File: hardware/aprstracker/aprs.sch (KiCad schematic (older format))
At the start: 98 parts

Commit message: [HW] Update schematics
Signed-off-by: Angel Hitov <angelhitov@gmail.com>
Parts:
- removed C? (x2): C, ~, symbol C
- removed R? (x2): R, ~, symbol R
- added C? (x15): C, ~, symbol C
- added C? (x2): CTRIM, ~, symbol CTRIM
- added C?: CAPAPOL, ~, symbol CAPAPOL
- added L? (x7): INDUCTOR, ~, symbol INDUCTOR
- added P?: BNC, ~, symbol BNC
- added Q?: NPN, ~, symbol NPN
- added R?: R, ~, symbol R
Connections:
- net labels removed: VRF
- wire segments 174 -> 183
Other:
- moved on the sheet: C?, Q?, R?

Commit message: [HW] Schematic update
Signed-off-by: Angel Hitov <angelhitov@gmail.com>
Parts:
- removed C? (x2): C, ~, symbol C
- removed L?: INDUCTOR, ~, symbol INDUCTOR
- removed P? (x2): BNC, ~, symbol BNC
- removed R? (x2): R, ~, symbol R
- added J1, J?: SMA, SMA, symbol SMA
- added L6: INDUCTOR, ~, symbol INDUCTOR
- added Q2: NPN, ~, symbol NPN
- added R14, R18: R, ~, symbol R
- Q3: renamed from Q?; value PNP -> BCX56
- Q4, Q5: renamed from Q?; value NPN -> BFR93A
- Q6: renamed from Q?; value NPN -> BFG135
- gave numbers to parts that had none: 111
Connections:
- net labels added: RF_EN
- net labels removed: VCO_EN
- wire segments 183 -> 187
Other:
- moved on the sheet: C19, Q3, R17, R20

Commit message: [HW] Kicad project adjustments
Signed-off-by: Angel Hitov <angelhitov@gmail.com>
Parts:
- gave numbers to parts that had none: 1
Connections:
- net CL is gone; now on net CE: U1.4 (CL)
- net CE: now also IC1.12 ((ICP)PB0), IC1.13 ((OC1A)PB1)
- net DATA: now also IC1.14 ((~SS~/OC1B)PB2)
- net GND: now also C48.2
- net at C16.1, C17.1, C18.1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: no longer R24.1
- net at Q5.1 (E), R26.1: now also R24.1
- no-connect marks 0 -> 24
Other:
- moved on the sheet: R24

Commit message: [HW] Schematics/footprints update
Signed-off-by: Angel Hitov <angelhitov@gmail.com>
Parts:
- removed U3: 78L33, ~, symbol 78L05
- removed U4: 78L05, ~, symbol 78L05
- added U3: 78L33, symbol 78LXX
- added U4: 78L05, symbol 78LXX
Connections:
- net +5V: now also U3.3 (VI)
- net GND: now also U3.2 (GND), U4.2 (GND)
- net VCC: now also U4.1 (VO)
- net VDD: now also U4.3 (VI)
- net at C43.1, C45.1, L15.1: now also U3.1 (VO)
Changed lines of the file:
@@
 LIBS:EB-3531
 LIBS:sma
+LIBS:78LXX_SMD
+LIBS:aprs
 LIBS:aprs-cache
 EELAYER 24 0
@@
 RF_EN
 $Comp
-L 78L05 U4
-U 1 1 51A2033B
-P 13550 1950
-F 0 "U4" H 13700 1754 60  0000 C CNN
-F 1 "78L05" H 13550 2150 60  0000 C CNN
-F 2 "~" H 13550 1950 60  0000 C CNN
-F 3 "~" H 13550 1950 60  0000 C CNN
-	1    13550 1950
-	1    0    0    -1
-$EndComp
-$Comp
 L CONN_2 P3
 U 1 1 51A20CAC
@@
 F 3 "~" H 13100 2200 300 0000 C CNN
 	1    13100 2200
-	1    0    0    -1
-$EndComp
-$Comp
-L 78L05 U3
-U 1 1 51A21285
-P 12150 2900
-F 0 "U3" H 12300 2704 60  0000 C CNN
-F 1 "78L33" H 12150 3100 60  0000 C CNN
-F 2 "~" H 12150 2900 60  0000 C CNN
-F 3 "~" H 12150 2900 60  0000 C CNN
-	1    12150 2900
 	1    0    0    -1
 $EndComp
@@
 Wire Wire Line
 	14250 1950 14250 1900
+$Comp
+L 78LXX U4
+U 1 1 51AB80B0
+P 13550 1950
+F 0 "U4" H 13700 1754 60  0000 C CNN
+F 1 "78L05" H 13550 2150 60  0000 C CNN
+F 2 "" H 13550 1950 60  0000 C CNN
+F 3 "" H 13550 1950 60  0000 C CNN
+	1    13550 1950
+	1    0    0    -1
+$EndComp
+$Comp
+L 78LXX U3
+U 1 1 51AB8477
+P 12150 2900
+F 0 "U3" H 12300 2704 60  0000 C CNN
+F 1 "78L33" H 12150 3100 60  0000 C CNN
+F 2 "" H 12150 2900 60  0000 C CNN
+F 3 "" H 12150 2900 60  0000 C CNN
+	1    12150 2900
+	1    0    0    -1
+$EndComp
 $EndSCHEMATC

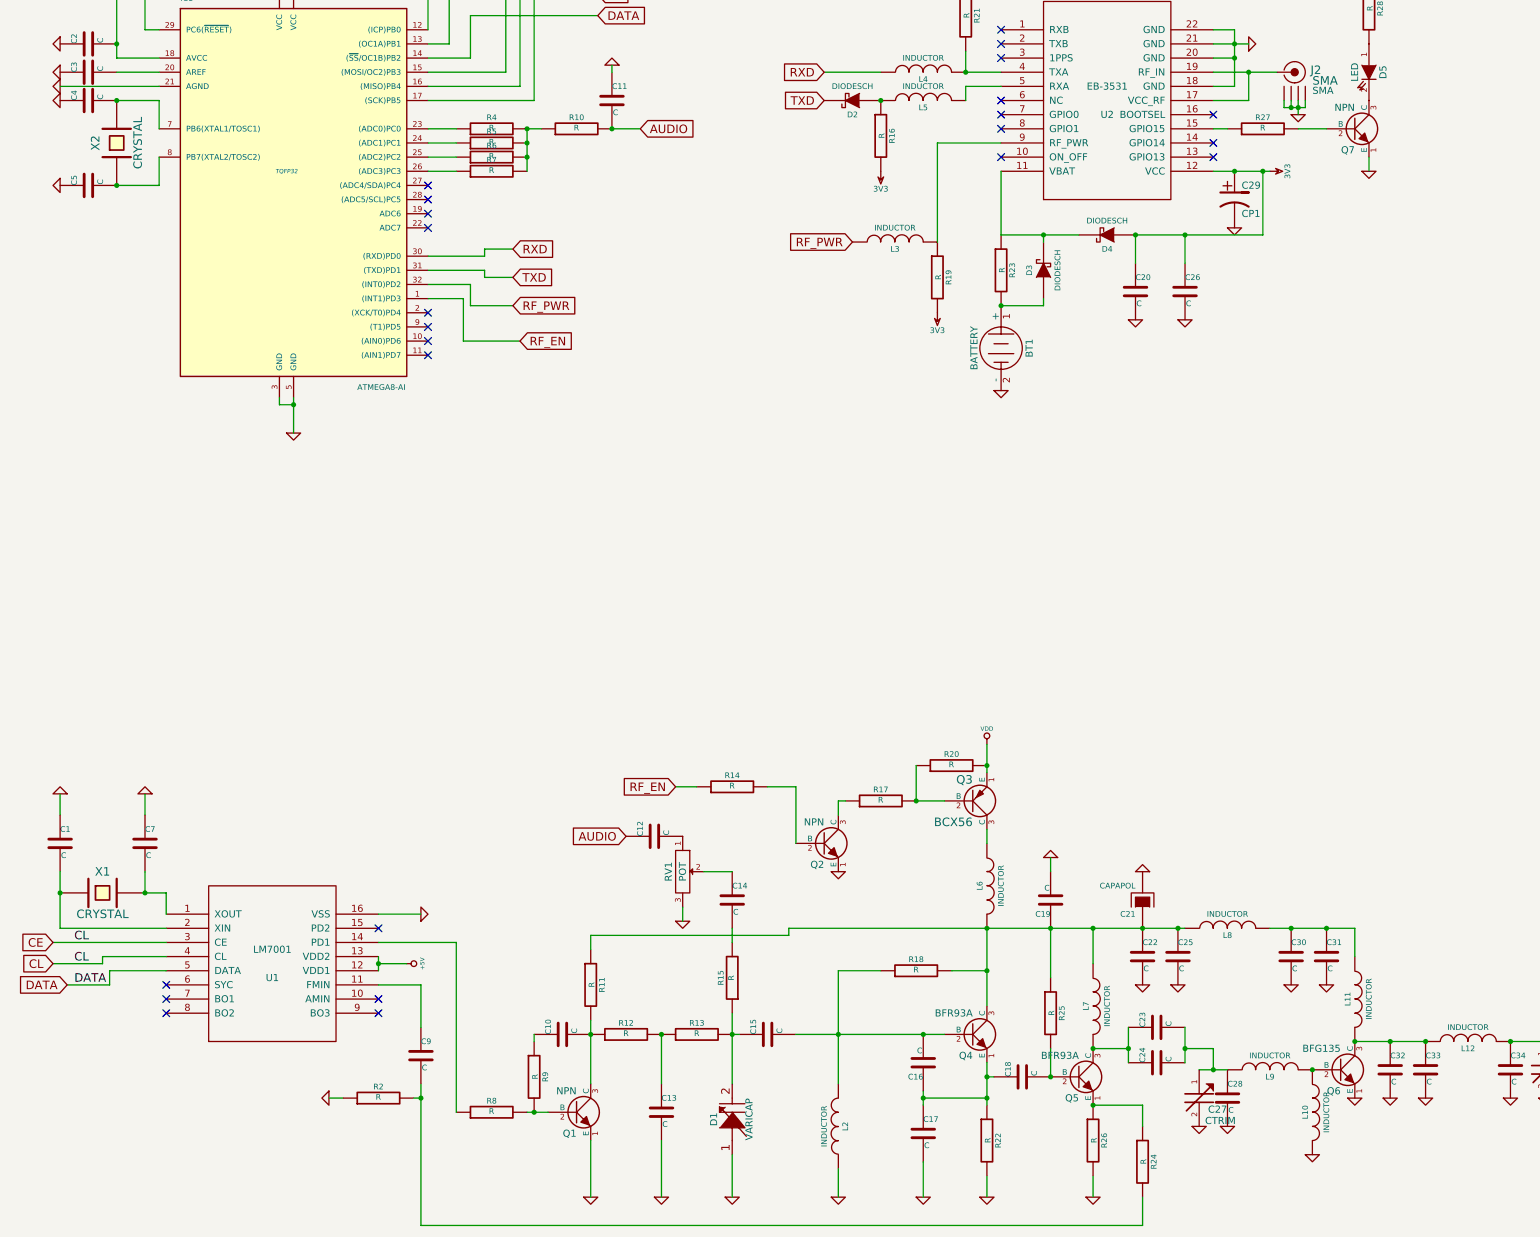
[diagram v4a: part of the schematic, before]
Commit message: [HW] Update pcb, rearrange components
Signed-off-by: Angel Hitov <angelhitov@gmail.com>
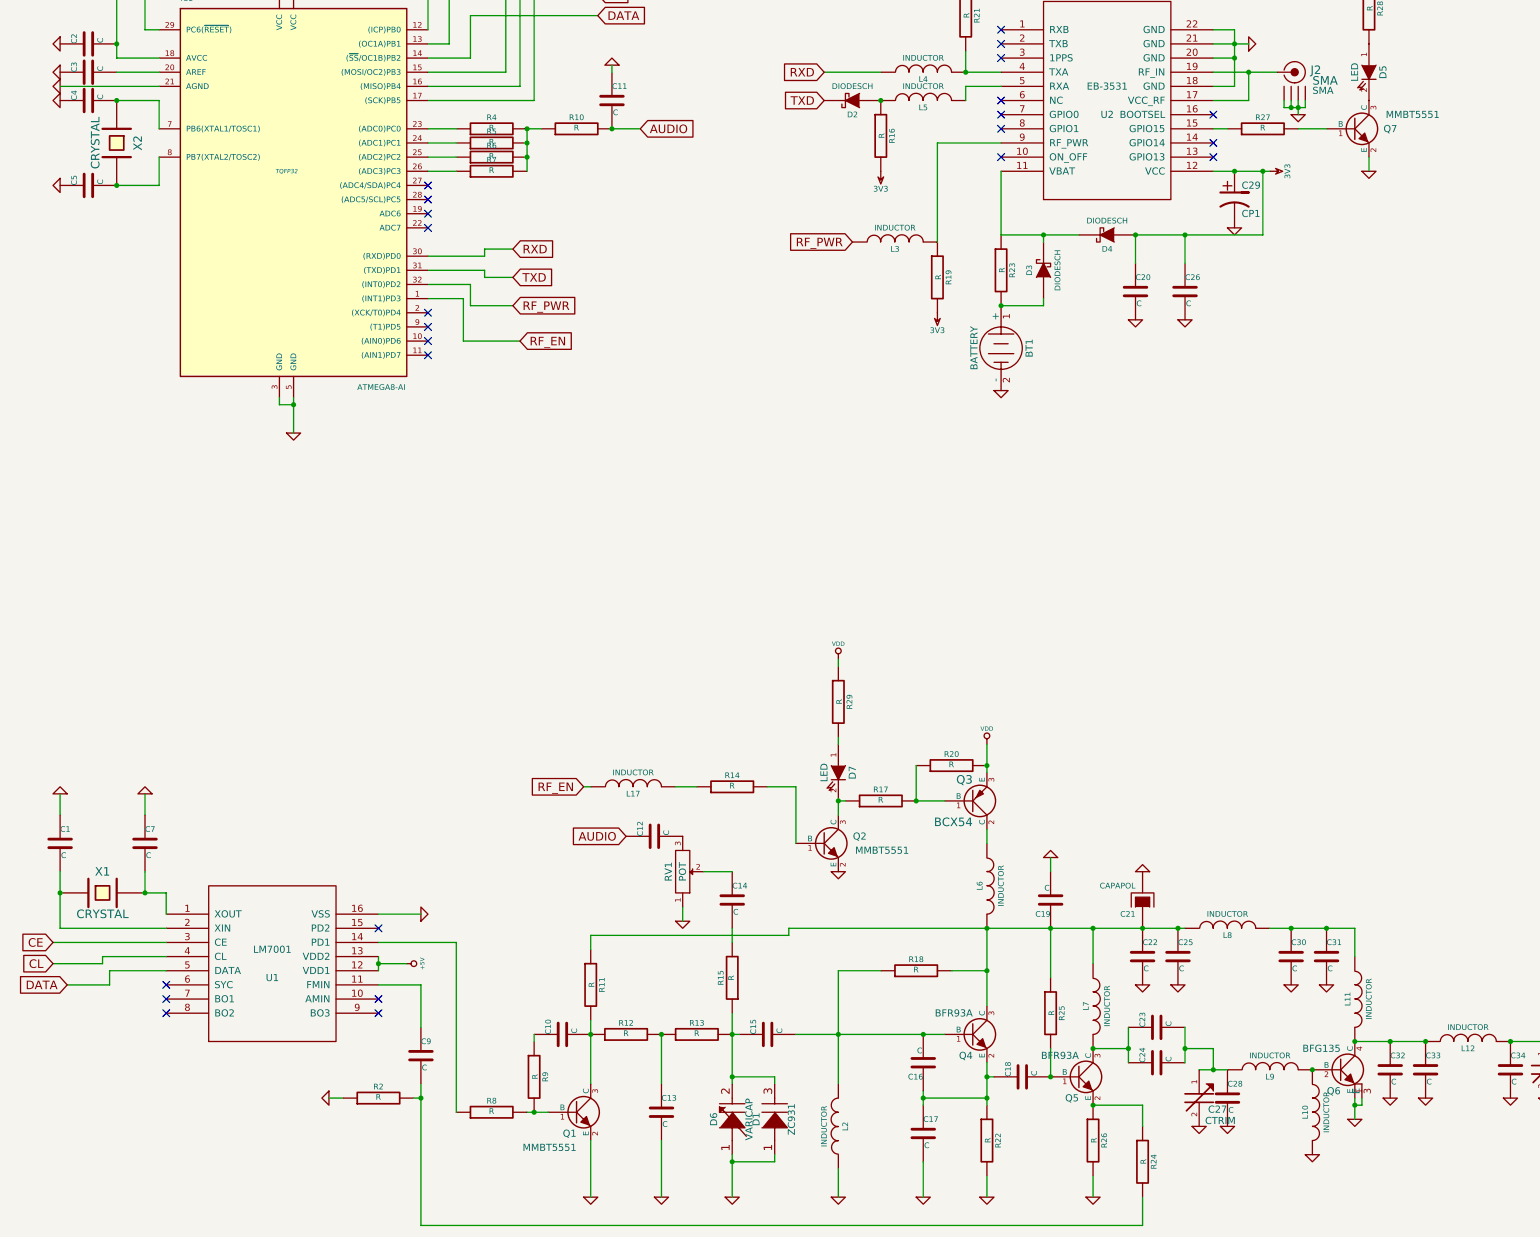
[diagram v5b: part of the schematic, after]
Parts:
- removed Q1, Q2, Q7: NPN, ~, symbol NPN
- removed Q3: BCX56, ~, symbol PNP
- removed Q4, Q5: BFR93A, ~, symbol NPN
- removed Q6: BFG135, ~, symbol NPN
- added D1: ZC931, symbol ZC931
- added D7: LED, symbol LED
- added L17: INDUCTOR, symbol INDUCTOR
- added Q1, Q2, Q7: MMBT5551, symbol MMBT5551
- added Q3: BCX54, symbol BCX54
- added Q4, Q5: BFR93A, symbol BFR93A
- added Q6: BFG135, symbol BFG135
- added R29: R, symbol R
- renumbered D1 to D6
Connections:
- net CE: no longer IC1.12 ((ICP)PB0), U1.4 (CL)
- net GND: now also RV1.1, D1.1 (ANODE), Q1.2 (E), Q2.2 (E), Q6.1 (E), Q6.3 (E), Q7.2 (E); no longer RV1.3
- net RF_EN: now also L17.1; no longer R14.1
- net VDD: now also Q3.3 (E), R29.1
- net at C16.1, C17.1, C18.1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: now also Q4.2 (E)
- net at C15.2, C16.2, L2.2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: now also Q4.1 (B)
- net at C19.1, C21.1, C22.1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: now also Q4.3 (C)
- net at C15.1, D6.2 (CATHODE), R13.2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: now also D1.3 (CATHODE)
- net at C10.2, R11.2, R12.1: now also Q1.3 (C)
- net at R8.2, R9.2: now also Q1.1 (B)
- net at R24.1, R26.1: now also Q5.2 (E)
- net at C18.2, R25.2: now also Q5.1 (B)
- net at C23.1, C24.1, L7.2: now also Q5.3 (C)
- net at R17.2, R20.1: now also Q3.1 (B)
- net at L6.1: now also Q3.2 (C)
- net at R17.1: now also D7.2 (K), Q2.3 (C)
- net at C12.2: now also RV1.3; no longer RV1.1
- net at C4.2, IC1.7 (PB6(XTAL1/TOSC1)): now also X2.1; no longer X2.2
- net at C5.2, IC1.8 (PB7(XTAL2/TOSC2)): now also X2.2; no longer X2.1
- net at R27.2: now also Q7.1 (B)
- net at D5.2 (K): now also Q7.3 (C)
- net at L10.1, L9.2: now also Q6.2 (B)
- net at C32.1, C33.1, L11.2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: now also Q6.4 (C)
- net at R14.2: now also Q2.1 (B)
- new net: L17.2, R14.1
- new net: D7.1 (A), R29.2
- new net CL: IC1.12 ((ICP)PB0), U1.4 (CL)
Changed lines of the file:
@@
 $EndDescr
-$Comp
-L NPN Q4
-U 1 1 519FACD7
-P 7350 9250
-F 0 "Q4" H 7350 9100 50  0000 R CNN
-F 1 "BFR93A" H 7350 9400 50  0000 R CNN
-F 2 "~" H 7350 9250 60  0000 C CNN
-F 3 "~" H 7350 9250 60  0000 C CNN
-	1    7350 9250
-	1    0    0    -1
-$EndComp
 $Comp
 L R R22
@@
 $EndComp
 $Comp
-L VARICAP D1
+L VARICAP D6
 U 1 1 519FD802
 P 5650 9850
-F 0 "D1" H 5650 9980 50  0000 C CNN
+F 0 "D6" H 5650 9980 50  0000 C CNN
 F 1 "VARICAP" H 5650 9730 50  0000 C CNN
 F 2 "~" H 5650 9850 60  0000 C CNN
@@
 	1    4900 9250
 	0    -1   -1   0
-$EndComp
-$Comp
-L NPN Q1
-U 1 1 519FDB7A
-P 4550 9800
-F 0 "Q1" H 4550 9650 50  0000 R CNN
-F 1 "NPN" H 4550 9950 50  0000 R CNN
-F 2 "~" H 4550 9800 60  0000 C CNN
-F 3 "~" H 4550 9800 60  0000 C CNN
-	1    4550 9800
-	1    0    0    -1
 $EndComp
 $Comp
@@
 $EndComp
 $Comp
-L NPN Q5
-U 1 1 519FF51E
-P 8100 9550
-F 0 "Q5" H 8100 9400 50  0000 R CNN
-F 1 "BFR93A" H 8100 9700 50  0000 R CNN
-F 2 "~" H 8100 9550 60  0000 C CNN
-F 3 "~" H 8100 9550 60  0000 C CNN
-	1    8100 9550
-	1    0    0    -1
-$EndComp
-$Comp
 L R R26
 U 1 1 519FF588
@@
 $EndComp
 $Comp
-L PNP Q3
-U 1 1 519FFC15
-P 7350 7600
-F 0 "Q3" H 7350 7450 60  0000 R CNN
-F 1 "BCX56" H 7350 7750 60  0000 R CNN
-F 2 "~" H 7350 7600 60  0001 C CNN
-F 3 "~" H 7350 7600 60  0000 C CNN
-	1    7350 7600
-	1    0    0    1
-$EndComp
-$Comp
 L R R20
 U 1 1 519FFCE4
@@
 	0    -1   -1   0
 $EndComp
-Text GLabel 5250 7500 0    60   Input ~ 0
+Text GLabel 4600 7500 0    60   Input ~ 0
 RF_EN
 $Comp
@@
 F 3 "~" H 5300 8100 60  0000 C CNN
 	1    5300 8100
-	0    1    1    0
+	0    1    -1   0
 $EndComp
 $Comp
@@
 F 3 "~" H 1300 2950 60  0000 C CNN
 	1    1300 2950
-	0    -1   -1   0
+	0    1    1    0
 $EndComp
 $Comp
@@
 $EndComp
 $Comp
-L NPN Q7
-U 1 1 51A0E2B5
-P 10050 2850
-F 0 "Q7" H 10050 2700 50  0000 R CNN
-F 1 "NPN" H 10050 3000 50  0000 R CNN
-F 2 "~" H 10050 2850 60  0000 C CNN
-F 3 "~" H 10050 2850 60  0000 C CNN
-	1    10050 2850
-	1    0    0    -1
-$EndComp
-$Comp
 L GND #PWR036
 U 1 1 51A0E37C
@@
 $EndComp
 $Comp
-L NPN Q6
-U 1 1 51A3A20A
-P 9950 9500
-F 0 "Q6" H 9950 9350 50  0000 R CNN
-F 1 "BFG135" H 9950 9650 50  0000 R CNN
-F 2 "~" H 9950 9500 60  0000 C CNN
-F 3 "~" H 9950 9500 60  0000 C CNN
-	1    9950 9500
-	1    0    0    -1
-$EndComp
-$Comp
 L INDUCTOR L11
 U 1 1 51A3A3B6
@@
 L GND #PWR054
 U 1 1 51A3AB43
-P 10050 9700
-F 0 "#PWR054" H 10050 9700 30  0001 C CNN
-F 1 "GND" H 10050 9630 30  0001 C CNN
-F 2 "" H 10050 9700 60  0000 C CNN
-F 3 "" H 10050 9700 60  0000 C CNN
-	1    10050 9700
+P 10050 9850
+F 0 "#PWR054" H 10050 9850 30  0001 C CNN
+F 1 "GND" H 10050 9780 30  0001 C CNN
+F 2 "" H 10050 9850 60  0000 C CNN
+F 3 "" H 10050 9850 60  0000 C CNN
+	1    10050 9850
 	1    0    0    -1
 $EndComp
@@
 Wire Wire Line
 	7900 8850 7900 8500
-$Comp
-L NPN Q2
-U 1 1 51A3DA96
-P 6300 7900
-F 0 "Q2" H 6300 7750 50  0000 R CNN
-F 1 "NPN" H 6300 8050 50  0000 R CNN
-F 2 "~" H 6300 7900 60  0000 C CNN
-F 3 "~" H 6300 7900 60  0000 C CNN
-	1    6300 7900
-	1    0    0    -1
-$EndComp
 Wire Wire Line
 	6400 7700 6400 7600
@@
 	8550 9750 8200 9750
 Connection ~ 8200 9750
-Text Label 1000 8900 0    60   ~ 0
-DATA
-Text Label 1000 8600 0    60   ~ 0
-CL
-Text Label 1000 8750 0    60   ~ 0
-CL
 Text GLabel 4700 1750 2    60   Input ~ 0
 CL
@@
 	1    0    0    -1
 $EndComp
+$Comp
+L BFG135 Q6
+U 1 1 51ACF8AC
+P 9950 9500
+F 0 "Q6" H 9950 9350 50  0000 R CNN
+F 1 "BFG135" H 9950 9650 50  0000 R CNN
+F 2 "" H 9950 9500 60  0000 C CNN
+F 3 "" H 9950 9500 60  0000 C CNN
+	1    9950 9500
+	1    0    0    -1
+$EndComp
+Wire Wire Line
+	10050 9700 10050 9850
+Wire Wire Line
+	10100 9700 10100 9750
+Wire Wire Line
+	10100 9750 10050 9750
+Connection ~ 10050 9750
+$Comp
+L BFR93A Q5
+U 1 1 51AD01CC
+P 8100 9550
+F 0 "Q5" H 8100 9400 50  0000 R CNN
+F 1 "BFR93A" H 8100 9700 50  0000 R CNN
+F 2 "" H 8100 9550 60  0000 C CNN
+F 3 "" H 8100 9550 60  0000 C CNN
+	1    8100 9550
+	1    0    0    -1
+$EndComp
+$Comp
+L BFR93A Q4
+U 1 1 51AD01F1
+P 7350 9250
+F 0 "Q4" H 7350 9100 50  0000 R CNN
+F 1 "BFR93A" H 7350 9400 50  0000 R CNN
+F 2 "" H 7350 9250 60  0000 C CNN
+F 3 "" H 7350 9250 60  0000 C CNN
+	1    7350 9250
+	1    0    0    -1
+$EndComp
+Wire Wire Line
+	5950 9600 5950 9550
+Wire Wire Line
+	5950 9550 5650 9550
+Connection ~ 5650 9550
+Wire Wire Line
+	5950 10100 5950 10150
+Wire Wire Line
+	5950 10150 5650 10150
+Connection ~ 5650 10150
+$Comp
+L ZC931 D1
+U 1 1 51AD137F
+P 5950 9850
+F 0 "D1" H 5950 9980 50  0000 C CNN
+F 1 "ZC931" H 5950 9730 50  0000 C CNN
+F 2 "" H 5950 9850 60  0000 C CNN
+F 3 "" H 5950 9850 60  0000 C CNN
+	1    5950 9850
+	0    -1   -1   0
+$EndComp
+$Comp
+L MMBT5551 Q1
+U 1 1 51AD1854
+P 4550 9800
+F 0 "Q1" H 4550 9650 50  0000 R CNN
+F 1 "MMBT5551" H 4550 9550 50  0000 R CNN
+F 2 "" H 4550 9800 60  0000 C CNN
+F 3 "" H 4550 9800 60  0000 C CNN
+	1    4550 9800
+	1    0    0    -1
+$EndComp
+$Comp
+L MMBT5551 Q7
+U 1 1 51AE2F85
+P 10050 2850
+F 0 "Q7" H 10350 2850 50  0000 R CNN
+F 1 "MMBT5551" H 10650 2950 50  0000 R CNN
+F 2 "" H 10050 2850 60  0000 C CNN
+F 3 "" H 10050 2850 60  0000 C CNN
+	1    10050 2850
+	1    0    0    -1
+$EndComp
+$Comp
+L BCX54 Q3
+U 1 1 51AE3A5F
+P 7350 7600
+F 0 "Q3" H 7350 7450 60  0000 R CNN
+F 1 "BCX54" H 7350 7750 60  0000 R CNN
+F 2 "" H 7350 7600 60  0000 C CNN
+F 3 "" H 7350 7600 60  0000 C CNN
+	1    7350 7600
+	1    0    0    1
+$EndComp
+$Comp
+L MMBT5551 Q2
+U 1 1 51AE3CFB
+P 6300 7900
+F 0 "Q2" H 6600 7950 50  0000 R CNN
+F 1 "MMBT5551" H 6900 7850 50  0000 R CNN
+F 2 "" H 6300 7900 60  0000 C CNN
+F 3 "" H 6300 7900 60  0000 C CNN
+	1    6300 7900
+	1    0    0    -1
+$EndComp
+$Comp
+L LED D7
+U 1 1 51AE455D
+P 6400 7400
+F 0 "D7" H 6400 7500 50  0000 C CNN
+F 1 "LED" H 6400 7300 50  0000 C CNN
+F 2 "" H 6400 7400 60  0000 C CNN
+F 3 "" H 6400 7400 60  0000 C CNN
+	1    6400 7400
+	0    1    1    0
+$EndComp
+Connection ~ 6400 7600
+$Comp
+L R R29
+U 1 1 51AE475B
+P 6400 6900
+F 0 "R29" V 6480 6900 40  0000 C CNN
+F 1 "R" V 6407 6901 40  0000 C CNN
+F 2 "" V 6330 6900 30  0000 C CNN
+F 3 "" H 6400 6900 30  0000 C CNN
+	1    6400 6900
+	1    0    0    -1
+$EndComp
+Wire Wire Line
+	6400 7150 6400 7200
+$Comp
+L VDD #PWR071
+U 1 1 51AE48A7
+P 6400 6600
+F 0 "#PWR071" H 6400 6700 30  0001 C CNN
+F 1 "VDD" H 6400 6710 30  0000 C CNN
+F 2 "" H 6400 6600 60  0000 C CNN
+F 3 "" H 6400 6600 60  0000 C CNN
+	1    6400 6600
+	1    0    0    -1
+$EndComp
+Wire Wire Line
+	6400 6650 6400 6600
+$Comp
+L INDUCTOR L17
+U 1 1 51AE52B1
+P 4950 7500
+F 0 "L17" V 4900 7500 40  0000 C CNN
+F 1 "INDUCTOR" V 5050 7500 40  0000 C CNN
+F 2 "" H 4950 7500 60  0000 C CNN
+F 3 "" H 4950 7500 60  0000 C CNN
+	1    4950 7500
+	0    -1   -1   0
+$EndComp
+Wire Wire Line
+	4650 7500 4600 7500
 $EndSCHEMATC

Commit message: [HW] Add uncommited changes / PCB updates
Signed-off-by: Angel Hitov <angelhitov@gmail.com>
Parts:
- removed C20, C48: C, ~, symbol C
- removed C36, C45, C47, C49: CAPAPOL, ~, symbol CAPAPOL
- added D8: LED, symbol LED
- added R30: R, symbol R
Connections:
- net VCC: now also R30.2
- net at C7.2, U1.1 (XOUT): now also X1.1; no longer X1.2
- net at C1.2, U1.2 (XIN): now also X1.2; no longer X1.1
- net at Q5.2 (E), R26.1: no longer R24.1
- net at IC1.11 ((AIN1)PD7): now also D8.2 (K)
- net at C23.1, C24.1, L7.2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: now also R24.1
- new net: D8.1 (A), R30.1
- no-connect marks 24 -> 23

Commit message: [HW] Update pcb/sch/gps
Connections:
- net GND: now also U2.10 (ON_OFF)
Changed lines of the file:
@@
 LIBS:78LXX_SMD
 LIBS:aprs
-LIBS:aprs-cache
 EELAYER 24 0
 EELAYER END
@@
 	8350 9750 8350 9350
 Connection ~ 8350 9350
+Wire Wire Line
+	7550 3050 7300 3050
+Wire Wire Line
+	7300 3050 7300 3350
+$Comp
+L GND #PWR?
+U 1 1 529A61AE
+P 7300 3350
+F 0 "#PWR?" H 7300 3350 30  0001 C CNN
+F 1 "GND" H 7300 3280 30  0001 C CNN
+F 2 "" H 7300 3350 60  0000 C CNN
+F 3 "" H 7300 3350 60  0000 C CNN
+	1    7300 3350
+	1    0    0    -1
+$EndComp
 $EndSCHEMATC

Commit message: [HW] Add schematics values
Signed-off-by: Angel Hitov <angelhitov@gmail.com>
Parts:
- C1, C4, C5, C7: value C -> 22pF
- C10, C14: value C -> 10nF
- C11: value C -> NA
- C12: value C -> 0R
- C15: value C -> 1nF
- C19, C2, C26, C3, C38, C39, C43, C46, C50, C52, C6, C8: value C -> 100nF
- C21, C41, C51: value CAPAPOL -> 100uF/25V
- C29: value CP1 -> 100uF/25V
- L1, L17, L3, L4, L5: value INDUCTOR -> 10uH
- L14, L15, L16: value INDUCTOR -> 0
- L6: value INDUCTOR -> 68uH
- P1: value CONN_6 -> AVR ISP
- P3: value CONN_2 -> POWER 12V
- R10: value R -> 200k
- R11: value R -> 1.5k
- R13, R15: value R -> 100k
- R14, R16, R19, R21, R27, R3: value R -> 10k
- R17, R20: value R -> 47k
- R18, R8: value R -> 27k
- R22: value R -> 510
- R23: value R -> 270
- R28, R30: value R -> 300
- R29: value R -> 4.7k
- R4: value R -> 1k
- R5: value R -> 2k
- R6, R9: value R -> 3.9k
- R7: value R -> 8.2k
- RV1: value POT -> 10k
- X1: value CRYSTAL -> 7.2Mhz
- X2: value CRYSTAL -> 14.7456Mhz
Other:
- note added: "APRS Tracker"
- note added: "LZ1ARM"
- note added: "v0.1.0"
- moved on the sheet: C1, C10, C12, C13, C14, C15, C16, C17, C18, C19, C21, C22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
